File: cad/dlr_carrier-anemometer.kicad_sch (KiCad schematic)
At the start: 9 parts, among them J13 ANEMO_M12_5P, U7 SP3485EN

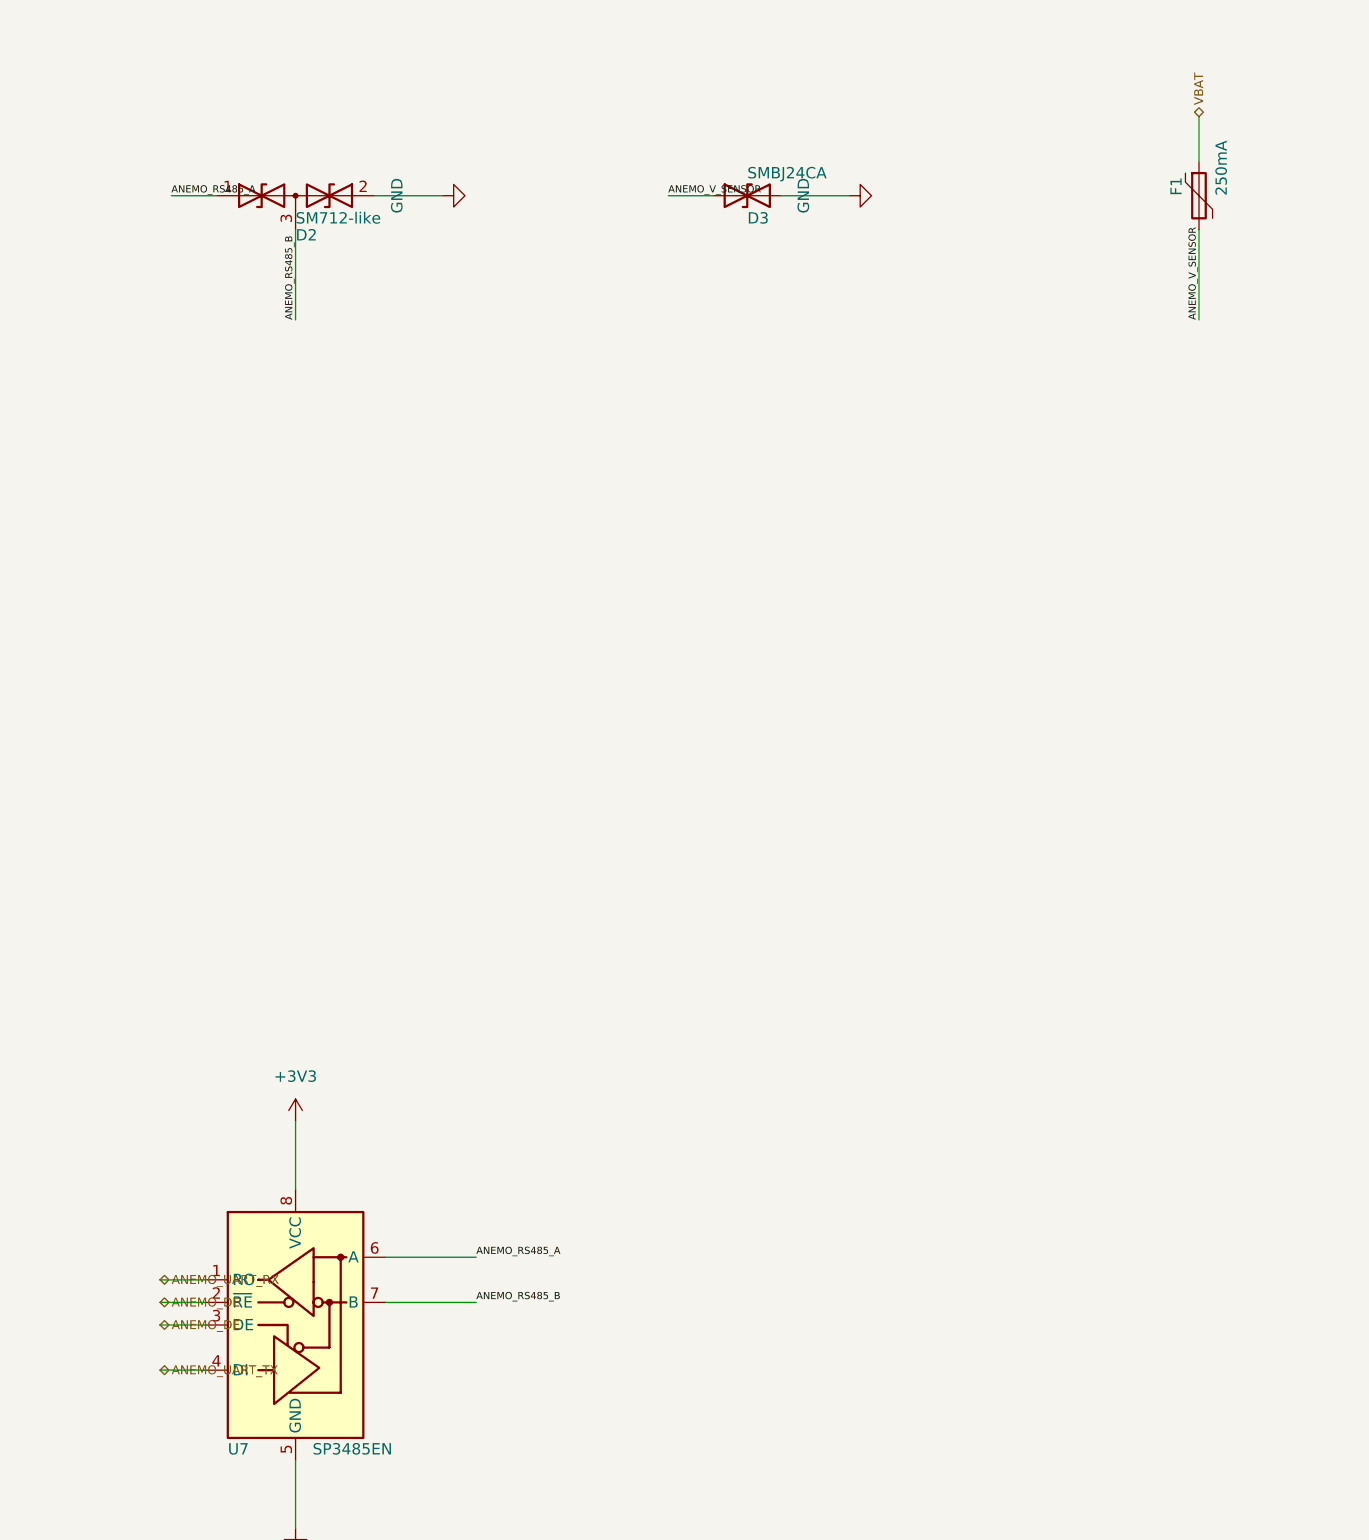
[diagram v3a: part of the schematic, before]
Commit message: 🩺 refactor(schematic): cross-sheet nets via global labels, no sheet pins
Three attempts at making the hierarchical sheet-pin mechanism pass KiCad 9 failed
(project name, instance paths, label type), so the mechanism goes. Cross-sheet nets
now connect by name through global labels on the child sheets; the root carries
sheet symbols only — no pins, no stub wires, no labels.

That removes the whole hier_label_mismatch / label_dangling class rather than
chasing it, and it matches the connectivity style the generate-schematic skill
already prescribes for this project ("all inter-block connections use net labels").

kicad-sch-api's add_global_label still does not serialize, so the labels are emitted
as hierarchical and rewritten in the saved sheet.

Co-Authored-By: Claude Opus 5 <noreply@anthropic.com>
Claude-Session: https://claude.ai/code/session_011xr7VCL7rkJj2WE2uQF7sF
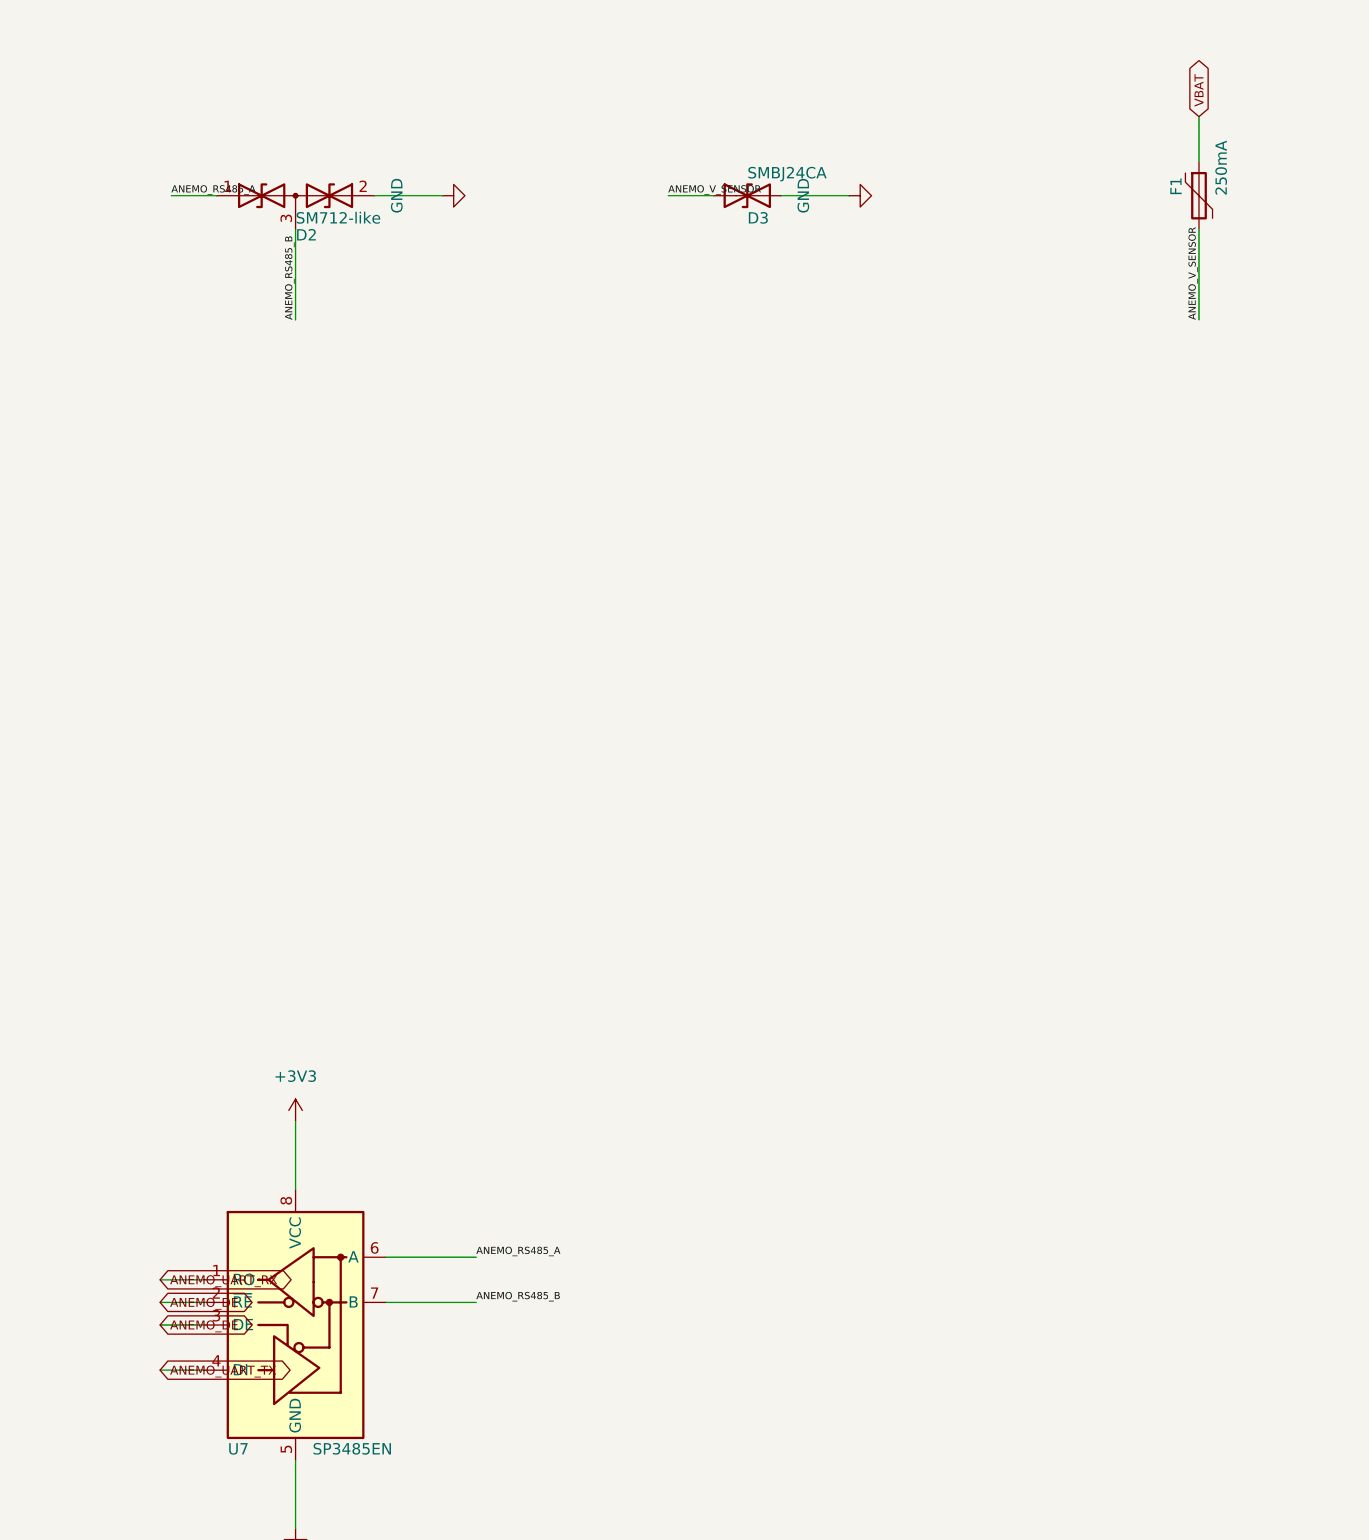
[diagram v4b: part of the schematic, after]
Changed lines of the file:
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@@
 		(instances
 			(project "ANEMOMETER RS-485"
-				(path "/6472ff61-5240-4a8c-a1e1-c967d2308f1e"
+				(path "/2156d267-d0ec-42fa-8c4f-1abdca0f48fc"
 					(reference "C30")
 					(unit 1)
@@
 		(instances
 			(project "ANEMOMETER RS-485"
-				(path "/6472ff61-5240-4a8c-a1e1-c967d2308f1e"
+				(path "/2156d267-d0ec-42fa-8c4f-1abdca0f48fc"
 					(reference "D2")
 					(unit 1)
@@
 		(instances
 			(project "ANEMOMETER RS-485"
-				(path "/6472ff61-5240-4a8c-a1e1-c967d2308f1e"
+				(path "/2156d267-d0ec-42fa-8c4f-1abdca0f48fc"
 					(reference "D3")
 					(unit 1)
@@
 		(instances
 			(project "ANEMOMETER RS-485"
-				(path "/6472ff61-5240-4a8c-a1e1-c967d2308f1e"
+				(path "/2156d267-d0ec-42fa-8c4f-1abdca0f48fc"
 					(reference "F1")
 					(unit 1)
@@
 		(instances
 			(project "ANEMOMETER RS-485"
-				(path "/6472ff61-5240-4a8c-a1e1-c967d2308f1e"
+				(path "/2156d267-d0ec-42fa-8c4f-1abdca0f48fc"
 					(reference "J13")
 					(unit 1)
@@
 		(instances
 			(project "ANEMOMETER RS-485"
-				(path "/6472ff61-5240-4a8c-a1e1-c967d2308f1e"
+				(path "/2156d267-d0ec-42fa-8c4f-1abdca0f48fc"
 					(reference "R14")
 					(unit 1)
@@
 		(instances
 			(project "ANEMOMETER RS-485"
-				(path "/6472ff61-5240-4a8c-a1e1-c967d2308f1e"
+				(path "/2156d267-d0ec-42fa-8c4f-1abdca0f48fc"
 					(reference "R15")
 					(unit 1)
@@
 		(instances
 			(project "ANEMOMETER RS-485"
-				(path "/6472ff61-5240-4a8c-a1e1-c967d2308f1e"
+				(path "/2156d267-d0ec-42fa-8c4f-1abdca0f48fc"
 					(reference "R16")
 					(unit 1)
@@
 		(instances
 			(project "ANEMOMETER RS-485"
-				(path "/6472ff61-5240-4a8c-a1e1-c967d2308f1e"
+				(path "/2156d267-d0ec-42fa-8c4f-1abdca0f48fc"
 					(reference "U7")
 					(unit 1)
@@
 		(instances
 			(project "ANEMOMETER RS-485"
-				(path "/6472ff61-5240-4a8c-a1e1-c967d2308f1e"
+				(path "/2156d267-d0ec-42fa-8c4f-1abdca0f48fc"
 					(reference "#PWR001")
 					(unit 1)
@@
 		(instances
 			(project "ANEMOMETER RS-485"
-				(path "/6472ff61-5240-4a8c-a1e1-c967d2308f1e"
+				(path "/2156d267-d0ec-42fa-8c4f-1abdca0f48fc"
 					(reference "#PWR002")
 					(unit 1)
@@
 		(instances
 			(project "ANEMOMETER RS-485"
-				(path "/6472ff61-5240-4a8c-a1e1-c967d2308f1e"
+				(path "/2156d267-d0ec-42fa-8c4f-1abdca0f48fc"
 					(reference "#PWR003")
 					(unit 1)
@@
 		(instances
 			(project "ANEMOMETER RS-485"
-				(path "/6472ff61-5240-4a8c-a1e1-c967d2308f1e"
+				(path "/2156d267-d0ec-42fa-8c4f-1abdca0f48fc"
 					(reference "#PWR004")
 					(unit 1)
@@
 		(instances
 			(project "ANEMOMETER RS-485"
-				(path "/6472ff61-5240-4a8c-a1e1-c967d2308f1e"
+				(path "/2156d267-d0ec-42fa-8c4f-1abdca0f48fc"
 					(reference "#PWR005")
 					(unit 1)
@@
 		(instances
 			(project "ANEMOMETER RS-485"
-				(path "/6472ff61-5240-4a8c-a1e1-c967d2308f1e"
+				(path "/2156d267-d0ec-42fa-8c4f-1abdca0f48fc"
 					(reference "#PWR006")
 					(unit 1)
@@
 		(instances
 			(project "ANEMOMETER RS-485"
-				(path "/6472ff61-5240-4a8c-a1e1-c967d2308f1e"
+				(path "/2156d267-d0ec-42fa-8c4f-1abdca0f48fc"
 					(reference "#PWR007")
 					(unit 1)
@@
 		(instances
 			(project "ANEMOMETER RS-485"
-				(path "/6472ff61-5240-4a8c-a1e1-c967d2308f1e"
+				(path "/2156d267-d0ec-42fa-8c4f-1abdca0f48fc"
 					(reference "#PWR008")
 					(unit 1)
@@
 		(instances
 			(project "ANEMOMETER RS-485"
-				(path "/6472ff61-5240-4a8c-a1e1-c967d2308f1e"
+				(path "/2156d267-d0ec-42fa-8c4f-1abdca0f48fc"
 					(reference "#PWR009")
 					(unit 1)
@@
 		(instances
 			(project "ANEMOMETER RS-485"
-				(path "/6472ff61-5240-4a8c-a1e1-c967d2308f1e"
+				(path "/2156d267-d0ec-42fa-8c4f-1abdca0f48fc"
 					(reference "#PWR010")
 					(unit 1)
@@
 		)
 	)
-	(hierarchical_label "ANEMO_DE"
+	(global_label "ANEMO_DE"
 		(shape bidirectional)
 		(at 99.06 226.06 180)
@@
 		)
 	)
-	(hierarchical_label "ANEMO_DE"
+	(global_label "ANEMO_DE"
 		(shape bidirectional)
 		(at 99.06 228.6 180)
@@
 		)
 	)
-	(hierarchical_label "ANEMO_UART_RX"
+	(global_label "ANEMO_UART_RX"
 		(shape bidirectional)
 		(at 99.06 223.52 180)
@@
 		)
 	)
-	(hierarchical_label "ANEMO_UART_TX"
+	(global_label "ANEMO_UART_TX"
 		(shape bidirectional)
 		(at 99.06 233.68 180)
@@
 		)
 	)
-	(hierarchical_label "VBAT"
+	(global_label "VBAT"
 		(shape bidirectional)
 		(at 215.9 92.71 90)
@@
 	)
 	(sheet_instances
-		(path "/e3ea6974-3a36-4b21-b0e6-499ff9f9e43f"
+		(path "/ac3b62a0-626f-4f89-acb3-1e4cb9b5f3dc"
 			(page "8")
 		)
